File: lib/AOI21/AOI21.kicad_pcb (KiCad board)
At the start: 2 copper layers, 6 parts

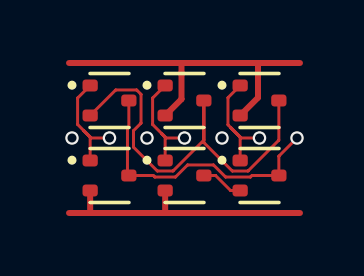
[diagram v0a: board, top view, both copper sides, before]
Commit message: High-density layout with pitch of 1.1mm, which gains 23% !!
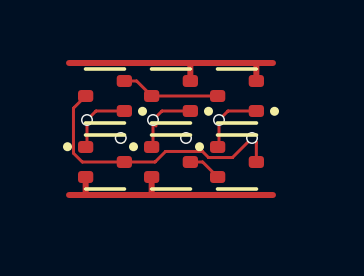
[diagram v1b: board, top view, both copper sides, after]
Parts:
- moved N3 0.87 mm to (5.50, 3.30)
- moved P3 0.76 mm to (5.50, 1.10), turned to 180 degrees
- moved N2 0.64 mm to (3.30, 3.30)
- moved N1 0.47 mm to (1.10, 3.30)
- moved P2 0.47 mm to (3.30, 1.10), turned to 180 degrees
- moved P1 0.21 mm to (1.10, 1.10), turned to 180 degrees
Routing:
- net intP: track 14.4 -> 3.32 mm
- net VDD: track 11.7 -> 8.00 mm
- net B2: track 4.04 -> 2.29 mm
- net A: track 3.91 -> 2.29 mm
- net B1: track 3.77 -> 2.53 mm
- net GND: track 9.20 -> 8.04 mm
- net (no net): vias 3 -> 2

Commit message: All cells now use 1mm*4mm grid rather than 1.1mm*4.4mm
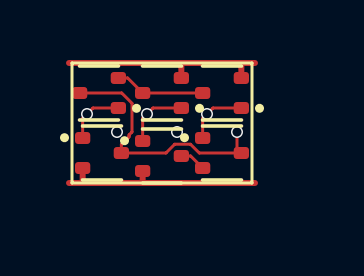
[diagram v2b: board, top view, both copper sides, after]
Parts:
- moved N3 0.58 mm to (5.00, 3.00)
- moved P3 0.51 mm to (5.00, 1.00)
- moved N2 0.36 mm to (3.00, 3.10)
- moved N1 0.32 mm to (1.00, 3.00)
- moved P2 0.32 mm to (3.00, 1.00)
- moved P1 0.22 mm to (0.90, 1.00)
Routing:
- net Y: track 9.51 -> 8.49 mm
- net GND: track 8.04 -> 7.15 mm
- net VDD: track 8.00 -> 7.24 mm

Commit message: Make the pads of my SOT523 footprint very slightly smaller, which is enough to route all the cells and leave the mosfets exactly on the grid
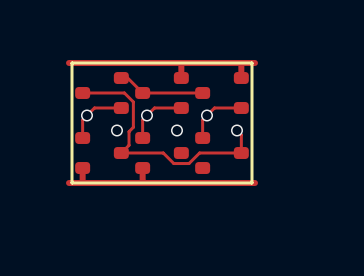
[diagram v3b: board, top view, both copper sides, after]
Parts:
- N1, N2, N3, P1, P2, P3: footprint Package_TO_SOT_SMD:SOT-523 -> RV523:SOT523
- moved N2 0.10 mm to (3.00, 3.00)
- moved P1 0.10 mm to (1.00, 1.00)
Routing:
- net intB: track 0.88 -> 0.00 mm

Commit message: Propagate MOSFET values to the cells' PCBs
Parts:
- N1, N2, N3: value (none) -> NMOS
- P1, P2, P3: value (none) -> PMOS
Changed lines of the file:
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@@
 			)
 		)
-		(property "Value" ""
+		(property "Value" "PMOS"
 			(at 0 0 180)
 			(layer "F.Fab")
@@
 			)
 		)
-		(property "Value" ""
+		(property "Value" "PMOS"
 			(at 0 0 180)
 			(layer "F.Fab")
@@
 			)
 		)
-		(property "Value" ""
+		(property "Value" "PMOS"
 			(at 0 0 180)
 			(layer "F.Fab")
@@
 			)
 		)
-		(property "Value" ""
+		(property "Value" "NMOS"
 			(at 0 0 0)
 			(layer "F.Fab")
@@
 			)
 		)
-		(property "Value" ""
+		(property "Value" "NMOS"
 			(at 0 0 0)
 			(layer "F.Fab")
@@
 			)
 		)
-		(property "Value" ""
-			(at 0 0 0)
-			(layer "F.Fab")
+		(property "Value" "NMOS"
+			(at 0 0 0)
+			(layer "F.Fab")

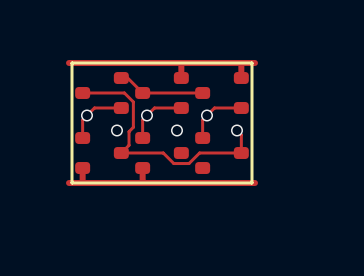
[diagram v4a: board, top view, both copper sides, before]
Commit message: Update AOI21 layout
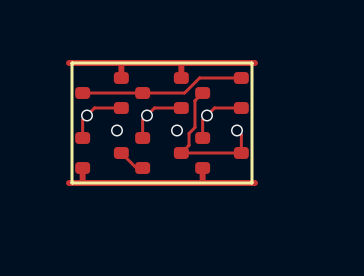
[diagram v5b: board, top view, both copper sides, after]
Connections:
- net A renamed A1
- N1 pad 3: Y -> sndA1
- N2 pad 1: B1 -> A2
- N2 pad 2: GND -> sndA1
- N2 pad 3: intB -> Y
- N3 pad 1: B2 -> B1
- N3 pad 2: intB -> GND
- P1 pad 2: intP -> VDD
- P1 pad 3: Y -> pndA
- P2 pad 1: B1 -> A2
- P2 pad 3: intP -> pndA
- P3 pad 1: B2 -> B1
- P3 pad 2: VDD -> pndA
- P3 pad 3: intP -> Y
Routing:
- net pndA: track 0.00 -> 5.50 mm
- net Y: track 8.78 -> 5.10 mm
- net intP: track 2.92 -> 0.00 mm
- net A2: track 0.00 -> 2.06 mm, vias 0 -> 1
- net B2: track 2.06 -> 0.00 mm, vias 1 -> 0
- net sndA1: track 0.00 -> 0.92 mm
